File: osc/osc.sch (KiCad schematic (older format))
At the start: 21 parts, among them P1 CONN_1, P2 CONN_1, P3 CONN_1, P4 CONN_1, P5 CONN_1, P6 CONN_5X2, Y1 ASOF3S3, Y2 AOCJYR, Y3 AST3TQ-28, Y4 M100

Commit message: Add Y4 footprint: SMT XO 5.0 x 3.2 mm
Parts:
- Y4: footprint (none) -> footprints:OSC5032
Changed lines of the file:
@@
 F 0 "Y4" H 7350 5350 60  0000 C CNN
 F 1 "M100" H 7300 4950 60  0000 L CNN
-F 2 "" H 7300 5300 60  0000 C CNN
+F 2 "footprints:OSC5032" H 7300 5300 60  0001 C CNN
 F 3 "" H 7300 5300 60  0000 C CNN
 	1    7550 5150

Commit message: Add Y3 footprint: SMT XO 7.0 x 5.0 mm
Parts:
- Y3: footprint (none) -> footprints:OSC7050
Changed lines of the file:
@@
 F 0 "Y3" H 7350 4550 60  0000 C CNN
 F 1 "AST3TQ-28" H 7300 4150 60  0000 L CNN
-F 2 "" H 7300 4500 60  0001 C CNN
+F 2 "footprints:OSC7050" H 7300 4500 60  0001 C CNN
 F 3 "" H 7300 4500 60  0000 C CNN
 	1    7550 4350

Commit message: All footprints are created and added to the schematic and the board.
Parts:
- Y1: footprint (none) -> footprints:OSC-ASOF3S3
- Y2: footprint (none) -> footprints:OSC-AOCJYR-SMT
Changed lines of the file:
@@
 F 0 "Y1" H 7350 3000 60  0000 C CNN
 F 1 "ASOF3S3" H 7300 2600 60  0000 L CNN
-F 2 "" H 7300 2950 60  0001 C CNN
+F 2 "footprints:OSC-ASOF3S3" H 7300 2950 60  0001 C CNN
 F 3 "" H 7300 2950 60  0000 C CNN
 	1    7550 2800
@@
 F 0 "Y2" H 7350 3800 60  0000 C CNN
 F 1 "AOCJYR" H 7300 3400 60  0000 L CNN
-F 2 "" H 7300 3750 60  0001 C CNN
+F 2 "footprints:OSC-AOCJYR-SMT" H 7300 3750 60  0001 C CNN
 F 3 "" H 7300 3750 60  0000 C CNN
 	1    7550 3600

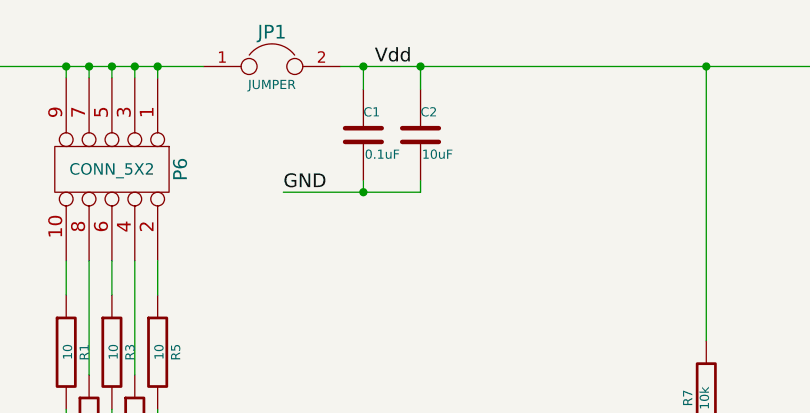
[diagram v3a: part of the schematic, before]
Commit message: Add an extra .1uF cap (build-time option, depends on the Osc assembled)
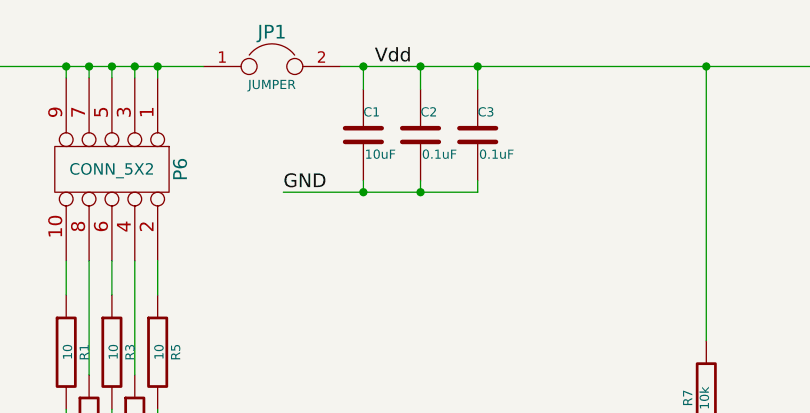
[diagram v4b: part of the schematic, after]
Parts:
- added C3: 0.1uF, Capacitors_SMD:C_0603, symbol C-RESCUE-osc
- renumbered C2 to C1, C1 to C2
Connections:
- net GND: now also C3.2
- net Vdd: now also C3.1
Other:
- moved on the sheet: C1, C2
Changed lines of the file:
@@
 	2900 5250 7100 5250
 $Comp
-L C-RESCUE-osc C1
+L C-RESCUE-osc C2
 U 1 1 557F00A8
-P 4850 2650
-F 0 "C1" H 4850 2750 40  0000 L CNN
-F 1 "0.1uF" H 4856 2565 40  0000 L CNN
-F 2 "Capacitors_SMD:C_0603" H 4888 2500 30  0001 C CNN
-F 3 "" H 4850 2650 60  0000 C CNN
-	1    4850 2650
+P 5100 2650
+F 0 "C2" H 5100 2750 40  0000 L CNN
+F 1 "0.1uF" H 5106 2565 40  0000 L CNN
+F 2 "Capacitors_SMD:C_0603" H 5138 2500 30  0001 C CNN
+F 3 "" H 5100 2650 60  0000 C CNN
+	1    5100 2650
 	1    0    0    -1
 $EndComp
@@
 $EndComp
 Wire Wire Line
-	4500 2900 5100 2900
+	4500 2900 5350 2900
 Wire Wire Line
 	4850 2900 4850 2850
@@
 $EndComp
 $Comp
-L C-RESCUE-osc C2
+L C-RESCUE-osc C1
 U 1 1 55F80AD1
-P 5100 2650
-F 0 "C2" H 5100 2750 40  0000 L CNN
-F 1 "10uF" H 5106 2565 40  0000 L CNN
-F 2 "Capacitors_SMD:C_1206" H 5138 2500 30  0001 C CNN
-F 3 "" H 5100 2650 60  0000 C CNN
-	1    5100 2650
+P 4850 2650
+F 0 "C1" H 4850 2750 40  0000 L CNN
+F 1 "10uF" H 4856 2565 40  0000 L CNN
+F 2 "Capacitors_SMD:C_1206" H 4888 2500 30  0001 C CNN
+F 3 "" H 4850 2650 60  0000 C CNN
+	1    4850 2650
 	1    0    0    -1
 $EndComp
@@
 	1    0    0    -1
 $EndComp
+$Comp
+L C-RESCUE-osc C3
+U 1 1 5711F01E
+P 5350 2650
+F 0 "C3" H 5350 2750 40  0000 L CNN
+F 1 "0.1uF" H 5356 2565 40  0000 L CNN
+F 2 "Capacitors_SMD:C_0603" H 5388 2500 30  0001 C CNN
+F 3 "" H 5350 2650 60  0000 C CNN
+	1    5350 2650
+	1    0    0    -1
+$EndComp
+Wire Wire Line
+	5350 2450 5350 2350
+Connection ~ 5350 2350
+Wire Wire Line
+	5350 2900 5350 2850
+Connection ~ 5100 2900
 $EndSCHEMATC

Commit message: Yet another .1uF cap.
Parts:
- added C4: 0.1uF, Capacitors_SMD:C_0603, symbol C-RESCUE-osc
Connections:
- net GND: now also C4.2
- net Vdd: now also C4.1
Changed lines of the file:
@@
 $EndComp
 Wire Wire Line
-	4500 2900 5350 2900
+	4500 2900 5600 2900
 Wire Wire Line
 	4850 2900 4850 2850
@@
 	5350 2900 5350 2850
 Connection ~ 5100 2900
+$Comp
+L C-RESCUE-osc C4
+U 1 1 5711F6C8
+P 5600 2650
+F 0 "C4" H 5600 2750 40  0000 L CNN
+F 1 "0.1uF" H 5606 2565 40  0000 L CNN
+F 2 "Capacitors_SMD:C_0603" H 5638 2500 30  0001 C CNN
+F 3 "" H 5600 2650 60  0000 C CNN
+	1    5600 2650
+	1    0    0    -1
+$EndComp
+Wire Wire Line
+	5600 2450 5600 2350
+Connection ~ 5600 2350
+Wire Wire Line
+	5600 2900 5600 2850
+Connection ~ 5350 2900
 $EndSCHEMATC

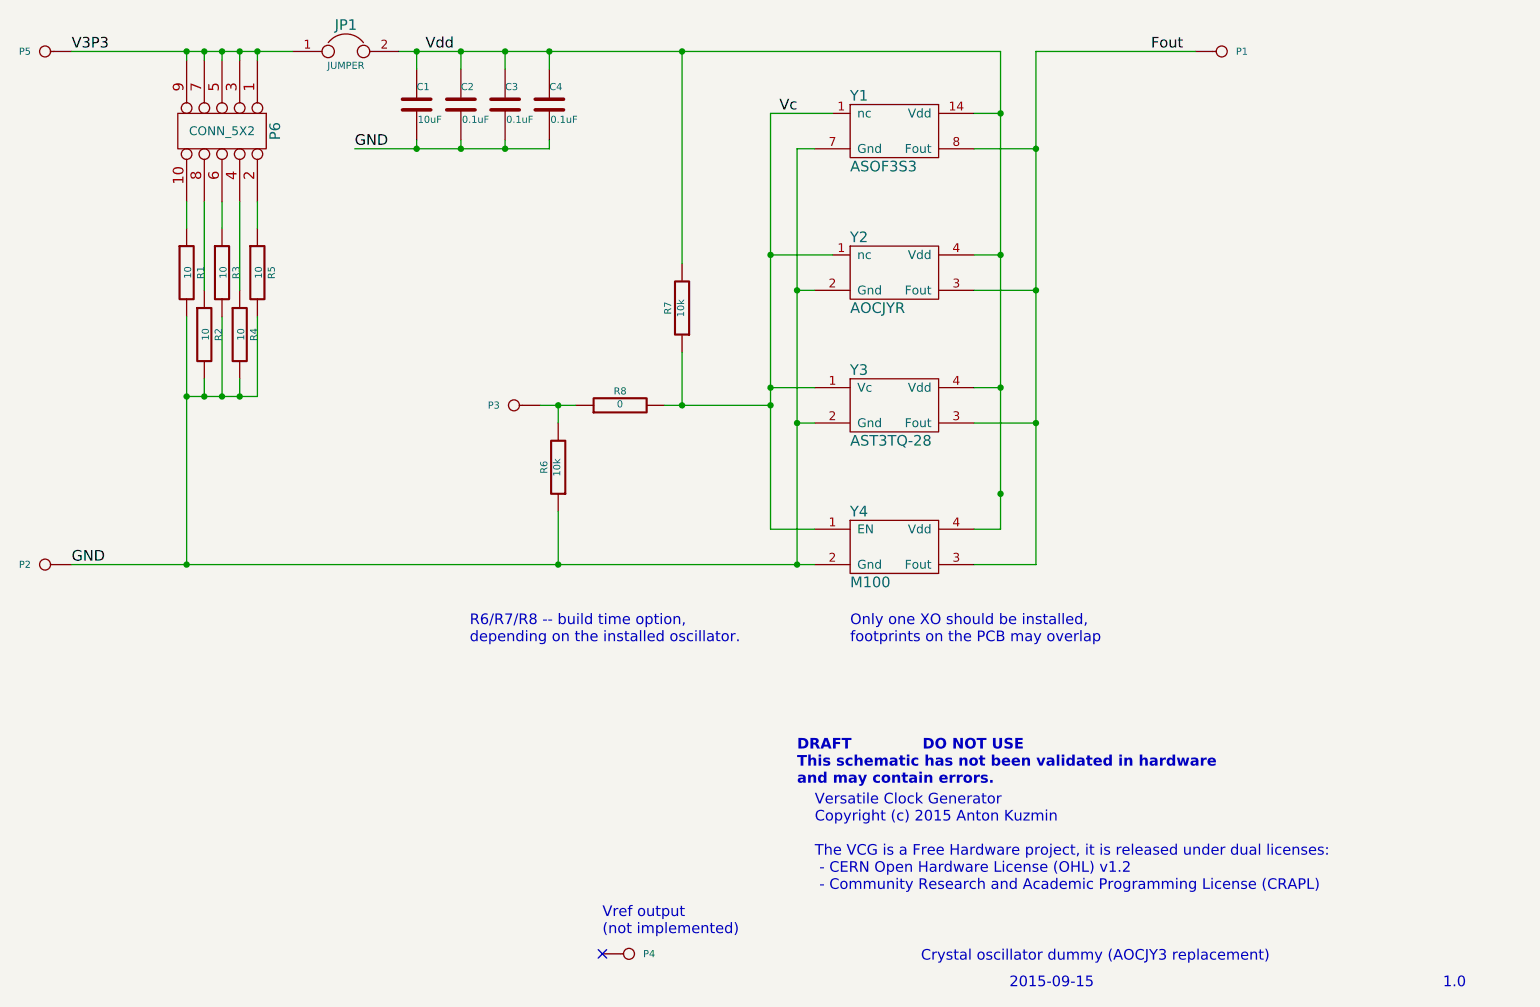
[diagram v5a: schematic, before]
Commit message: Refactor oscillator board before releasing to manufacturing: trace width, combine headers to a single part, etc.
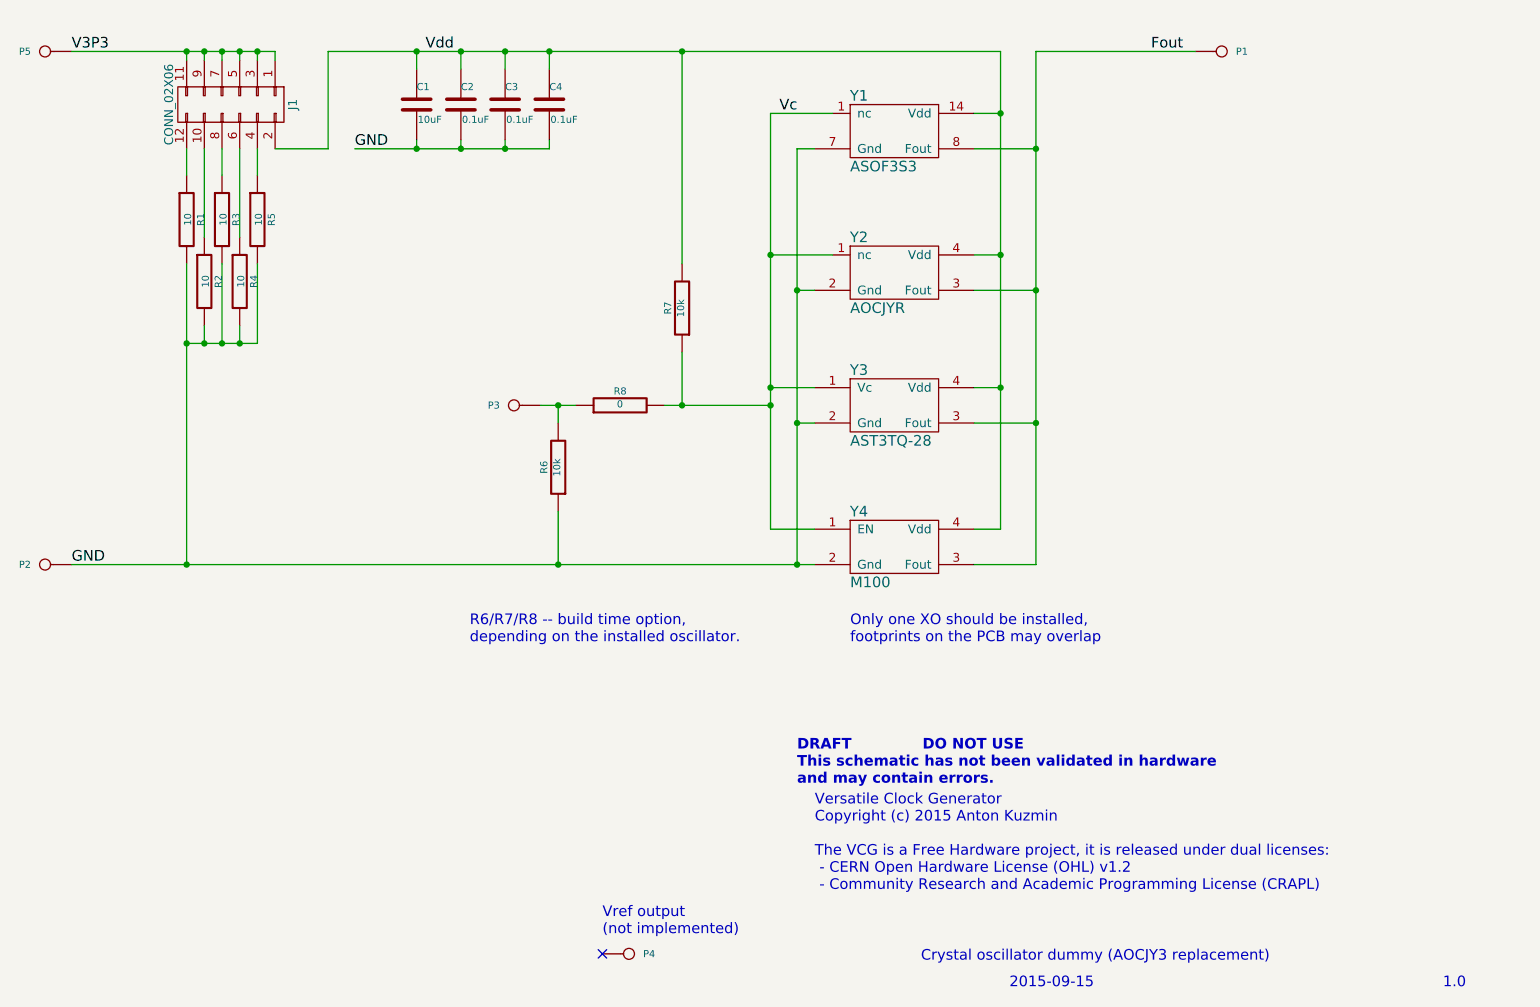
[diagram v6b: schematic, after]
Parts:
- removed JP1: JUMPER, Pin_Headers:Pin_Header_Straight_1x02, symbol JUMPER
- removed P6: CONN_5X2, Pin_Headers:Pin_Header_Straight_2x05, symbol CONN_5X2
- added J1: CONN_02X06, Pin_Headers:Pin_Header_Straight_2x06_Pitch2.54mm, symbol CONN_02X06
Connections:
- net V3P3: now also J1.1 (P1), J1.11 (P11), J1.3 (P3), J1.5 (P5), J1.7 (P7), J1.9 (P9)
- net Vdd: now also J1.2 (P2)
- net at R1.1: now also J1.12 (P12)
- net at R5.1: now also J1.4 (P4)
- net at R4.1: now also J1.6 (P6)
- net at R3.1: now also J1.8 (P8)
- net at R2.1: now also J1.10 (P10)
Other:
- moved on the sheet: R1, R2, R3, R4, R5
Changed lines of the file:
@@
-$EndComp
-$Comp
-L CONN_5X2 P6
-U 1 1 557EFB4D
-P 3750 2800
-F 0 "P6" H 3750 3100 60  0000 C CNN
-F 1 "CONN_5X2" V 3750 2800 50  0000 C CNN
-F 2 "Pin_Headers:Pin_Header_Straight_2x05" H 3750 2800 60  0001 C CNN
-F 3 "" H 3750 2800 60  0000 C CNN
-	1    3750 2800
-	0    1    1    0
 $EndComp
 $Comp
 L R-RESCUE-osc R1
 U 1 1 557EFBA9
-P 3550 3600
-F 0 "R1" V 3630 3600 40  0000 C CNN
-F 1 "10" V 3557 3601 40  0000 C CNN
-F 2 "Resistors_SMD:R_2512_HandSoldering" V 3480 3600 30  0001 C CNN
-F 3 "" H 3550 3600 30  0000 C CNN
-	1    3550 3600
+P 3550 3300
+F 0 "R1" V 3630 3300 40  0000 C CNN
+F 1 "10" V 3557 3301 40  0000 C CNN
+F 2 "Resistors_SMD:R_2512_HandSoldering" V 3480 3300 30  0001 C CNN
+F 3 "" H 3550 3300 30  0000 C CNN
+	1    3550 3300
 	1    0    0    -1
 $EndComp
@@
 L R-RESCUE-osc R2
 U 1 1 557EFC54
-P 3650 3950
-F 0 "R2" V 3730 3950 40  0000 C CNN
-F 1 "10" V 3657 3951 40  0000 C CNN
-F 2 "Resistors_SMD:R_2512_HandSoldering" V 3580 3950 30  0001 C CNN
-F 3 "" H 3650 3950 30  0000 C CNN
-	1    3650 3950
+P 3650 3650
+F 0 "R2" V 3730 3650 40  0000 C CNN
+F 1 "10" V 3657 3651 40  0000 C CNN
+F 2 "Resistors_SMD:R_2512_HandSoldering" V 3580 3650 30  0001 C CNN
+F 3 "" H 3650 3650 30  0000 C CNN
+	1    3650 3650
 	1    0    0    -1
 $EndComp
@@
 L R-RESCUE-osc R3
 U 1 1 557EFCC8
-P 3750 3600
-F 0 "R3" V 3830 3600 40  0000 C CNN
-F 1 "10" V 3757 3601 40  0000 C CNN
-F 2 "Resistors_SMD:R_2512_HandSoldering" V 3680 3600 30  0001 C CNN
-F 3 "" H 3750 3600 30  0000 C CNN
-	1    3750 3600
+P 3750 3300
+F 0 "R3" V 3830 3300 40  0000 C CNN
+F 1 "10" V 3757 3301 40  0000 C CNN
+F 2 "Resistors_SMD:R_2512_HandSoldering" V 3680 3300 30  0001 C CNN
+F 3 "" H 3750 3300 30  0000 C CNN
+	1    3750 3300
 	1    0    0    -1
 $EndComp
@@
 L R-RESCUE-osc R4
 U 1 1 557EFD0B
-P 3850 3950
-F 0 "R4" V 3930 3950 40  0000 C CNN
-F 1 "10" V 3857 3951 40  0000 C CNN
-F 2 "Resistors_SMD:R_2512_HandSoldering" V 3780 3950 30  0001 C CNN
-F 3 "" H 3850 3950 30  0000 C CNN
-	1    3850 3950
+P 3850 3650
+F 0 "R4" V 3930 3650 40  0000 C CNN
+F 1 "10" V 3857 3651 40  0000 C CNN
+F 2 "Resistors_SMD:R_2512_HandSoldering" V 3780 3650 30  0001 C CNN
+F 3 "" H 3850 3650 30  0000 C CNN
+	1    3850 3650
 	1    0    0    -1
 $EndComp
@@
 L R-RESCUE-osc R5
 U 1 1 557EFD39
-P 3950 3600
-F 0 "R5" V 4030 3600 40  0000 C CNN
-F 1 "10" V 3957 3601 40  0000 C CNN
-F 2 "Resistors_SMD:R_2512_HandSoldering" V 3880 3600 30  0001 C CNN
-F 3 "" H 3950 3600 30  0000 C CNN
-	1    3950 3600
-	1    0    0    -1
-$EndComp
-Wire Wire Line
-	3550 3200 3550 3350
-Wire Wire Line
-	3650 3700 3650 3200
-Wire Wire Line
-	3750 3200 3750 3350
-Wire Wire Line
-	3850 3200 3850 3700
-Wire Wire Line
-	3950 3200 3950 3350
-Wire Wire Line
-	2900 2350 4150 2350
+P 3950 3300
+F 0 "R5" V 4030 3300 40  0000 C CNN
+F 1 "10" V 3957 3301 40  0000 C CNN
+F 2 "Resistors_SMD:R_2512_HandSoldering" V 3880 3300 30  0001 C CNN
+F 3 "" H 3950 3300 30  0000 C CNN
+	1    3950 3300
+	1    0    0    -1
+$EndComp
+Wire Wire Line
+	3550 2900 3550 3050
+Wire Wire Line
+	3650 3400 3650 2900
+Wire Wire Line
+	3750 2900 3750 3050
+Wire Wire Line
+	3850 2900 3850 3400
+Wire Wire Line
+	3950 2900 3950 3050
 Wire Wire Line
 	3550 2350 3550 2400
@@
 Text Notes 10650 7650 0    60   ~ 0
 1.0
-$Comp
-L JUMPER JP1
-U 1 1 557F292B
-P 4450 2350
-F 0 "JP1" H 4450 2500 60  0000 C CNN
-F 1 "JUMPER" H 4450 2270 40  0000 C CNN
-F 2 "Pin_Headers:Pin_Header_Straight_1x02" H 4450 2350 60  0001 C CNN
-F 3 "" H 4450 2350 60  0000 C CNN
-	1    4450 2350
-	1    0    0    -1
-$EndComp
 Wire Wire Line
 	4500 2900 5600 2900
@@
 Connection ~ 3950 2350
 Wire Wire Line
-	4750 2350 8150 2350
+	4350 2350 8150 2350
 Wire Wire Line
 	4850 2350 4850 2450
@@
 	8000 2700 8150 2700
 Connection ~ 8150 2700
-Connection ~ 8150 4850
 Wire Wire Line
 	8000 2900 8350 2900
@@
 Connection ~ 8350 2900
 Wire Wire Line
-	3550 3850 3550 5250
+	3550 3550 3550 5250
 Connection ~ 3550 5250
 Wire Wire Line
-	3550 4300 3950 4300
-Wire Wire Line
-	3650 4300 3650 4200
-Connection ~ 3550 4300
-Wire Wire Line
-	3750 4300 3750 3850
-Connection ~ 3650 4300
-Wire Wire Line
-	3850 4300 3850 4200
-Connection ~ 3750 4300
-Wire Wire Line
-	3950 4300 3950 3850
-Connection ~ 3850 4300
+	3550 4000 3950 4000
+Wire Wire Line
+	3650 4000 3650 3900
+Connection ~ 3550 4000
+Wire Wire Line
+	3750 4000 3750 3550
+Connection ~ 3650 4000
+Wire Wire Line
+	3850 4000 3850 3900
+Connection ~ 3750 4000
+Wire Wire Line
+	3950 4000 3950 3550
+Connection ~ 3850 4000
 Text Notes 7300 5700 0    60   ~ 0
 Only one XO should be installed,\nfootprints on the PCB may overlap
@@
 	5600 2900 5600 2850
 Connection ~ 5350 2900
+$Comp
+L CONN_02X06 J1
+U 1 1 59A12FA4
+P 3800 2650
+F 0 "J1" H 3800 3000 50  0000 C CNN
+F 1 "CONN_02X06" H 3800 2300 50  0000 C CNN
+F 2 "Pin_Headers:Pin_Header_Straight_2x06_Pitch2.54mm" H 3800 1450 50  0001 C CNN
+F 3 "" H 3800 1450 50  0001 C CNN
+	1    3800 2650
+	0    1    1    0
+$EndComp
+Wire Wire Line
+	2900 2350 4050 2350
+Wire Wire Line
+	4050 2350 4050 2400
+Wire Wire Line
+	4050 2900 4350 2900
+Wire Wire Line
+	4350 2900 4350 2350
 $EndSCHEMATC
